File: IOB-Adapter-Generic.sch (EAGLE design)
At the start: 5 parts

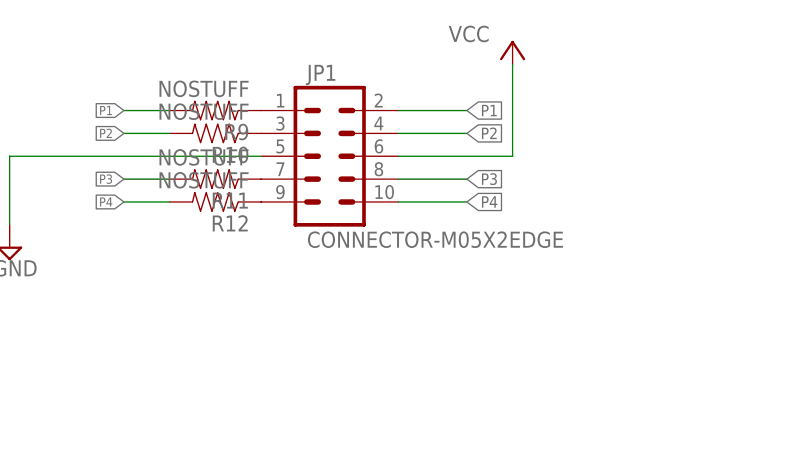
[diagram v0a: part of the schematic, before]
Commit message: change from edge to PTH mount
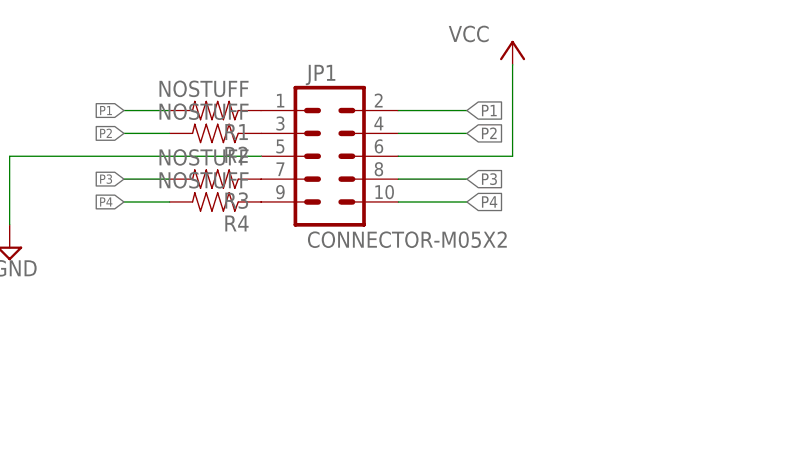
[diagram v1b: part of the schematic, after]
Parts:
- JP1: value CONNECTOR-M05X2EDGE -> CONNECTOR-M05X2; device SPCoast:CONNECTOR-M05X2EDGE -> SPCoast:CONNECTOR-M05X2
- renumbered R10 to R2, R11 to R3, R12 to R4, R9 to R1
